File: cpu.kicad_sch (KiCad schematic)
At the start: 19 parts, among them J1 FTSH-105-01-L-DV-K, J24 HTSW-103-07-G-S, U2 CC1312R1F3RGZR, Y2 OW7EL89CANUXK7YLC-48M

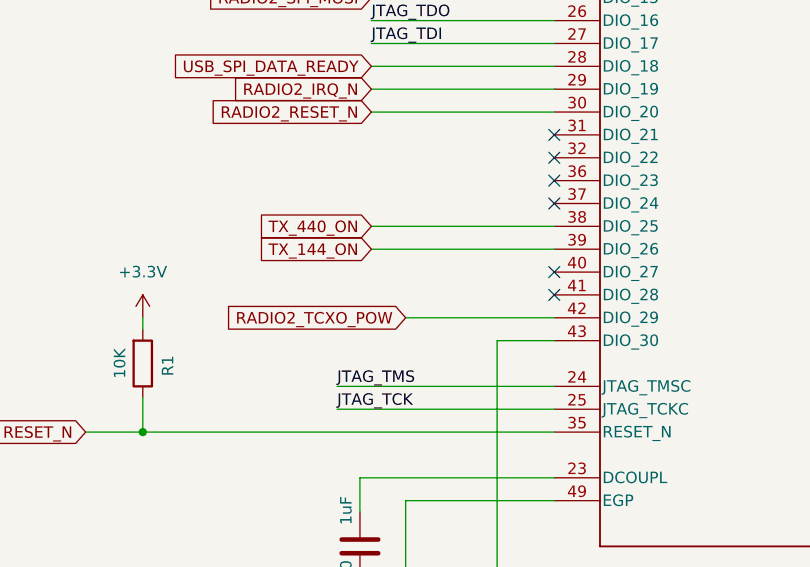
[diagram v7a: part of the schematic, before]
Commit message: Add thermsistors by the PAs
Signed-off-by: Corey Minyard <corey@minyard.net>
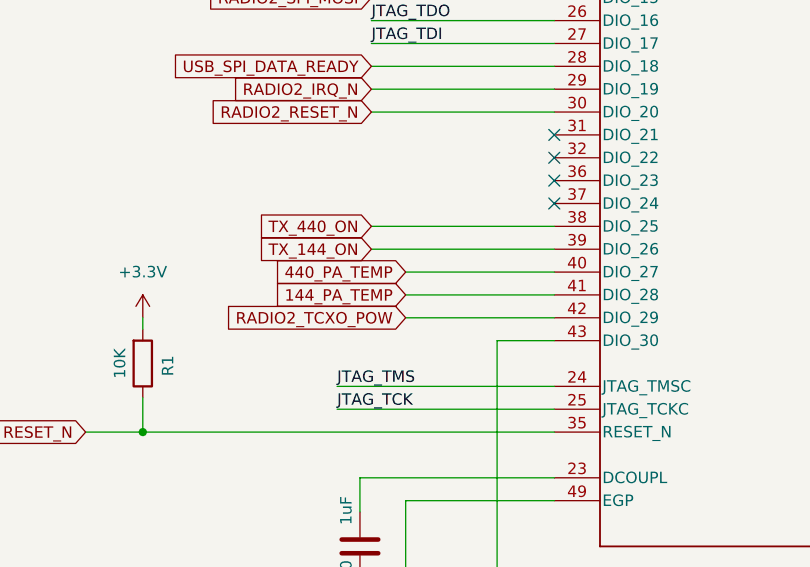
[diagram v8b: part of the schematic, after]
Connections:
- net 440_PA_TEMP: now reaches U2.40 (DIO_27)
- net 144_PA_TEMP: now reaches U2.41 (DIO_28)
- no-connect marks 10 -> 8
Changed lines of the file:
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@@
-	)
-	(no_connect
-		(at 78.74 118.11)
 	)
 	(no_connect
@@
 	)
 	(no_connect
-		(at 78.74 120.65)
-	)
-	(no_connect
 		(at 139.7 162.56)
 	)
@@
 	(wire
 		(pts
+			(xy 62.23 120.65) (xy 78.74 120.65)
+		)
+		(stroke
+			(width 0)
+			(type default)
+		)
+	)
+	(wire
+		(pts
 			(xy 212.09 59.69) (xy 245.11 59.69)
 		)
@@
 		(pts
 			(xy 156.21 69.85) (xy 156.21 80.01)
+		)
+		(stroke
+			(width 0)
+			(type default)
+		)
+	)
+	(wire
+		(pts
+			(xy 62.23 118.11) (xy 78.74 118.11)
 		)
 		(stroke
@@
 		)
 	)
+	(global_label "440_PA_TEMP"
+		(shape input)
+		(at 62.23 118.11 180)
+		(fields_autoplaced yes)
+		(effects
+			(font
+				(size 1.27 1.27)
+			)
+			(justify right)
+		)
+		(property "Intersheetrefs" "${INTERSHEET_REFS}"
+			(at 46.4845 118.11 0)
+			(effects
+				(font
+					(size 1.27 1.27)
+				)
+				(justify right)
+				(hide yes)
+			)
+		)
+	)
 	(global_label "RADIO2_RESET_N"
 		(shape input)
@@
 			(effects
 				(font
+					(size 1.27 1.27)
+				)
+				(justify right)
+				(hide yes)
+			)
+		)
+	)
+	(global_label "144_PA_TEMP"
+		(shape input)
+		(at 62.23 120.65 180)
+		(fields_autoplaced yes)
+		(effects
+			(font
+				(size 1.27 1.27)
+			)
+			(justify right)
+		)
+		(property "Intersheetrefs" "${INTERSHEET_REFS}"
+			(at 46.4845 120.65 0)
+			(effects
+				(font
